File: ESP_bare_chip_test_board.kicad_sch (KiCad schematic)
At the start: 0 parts

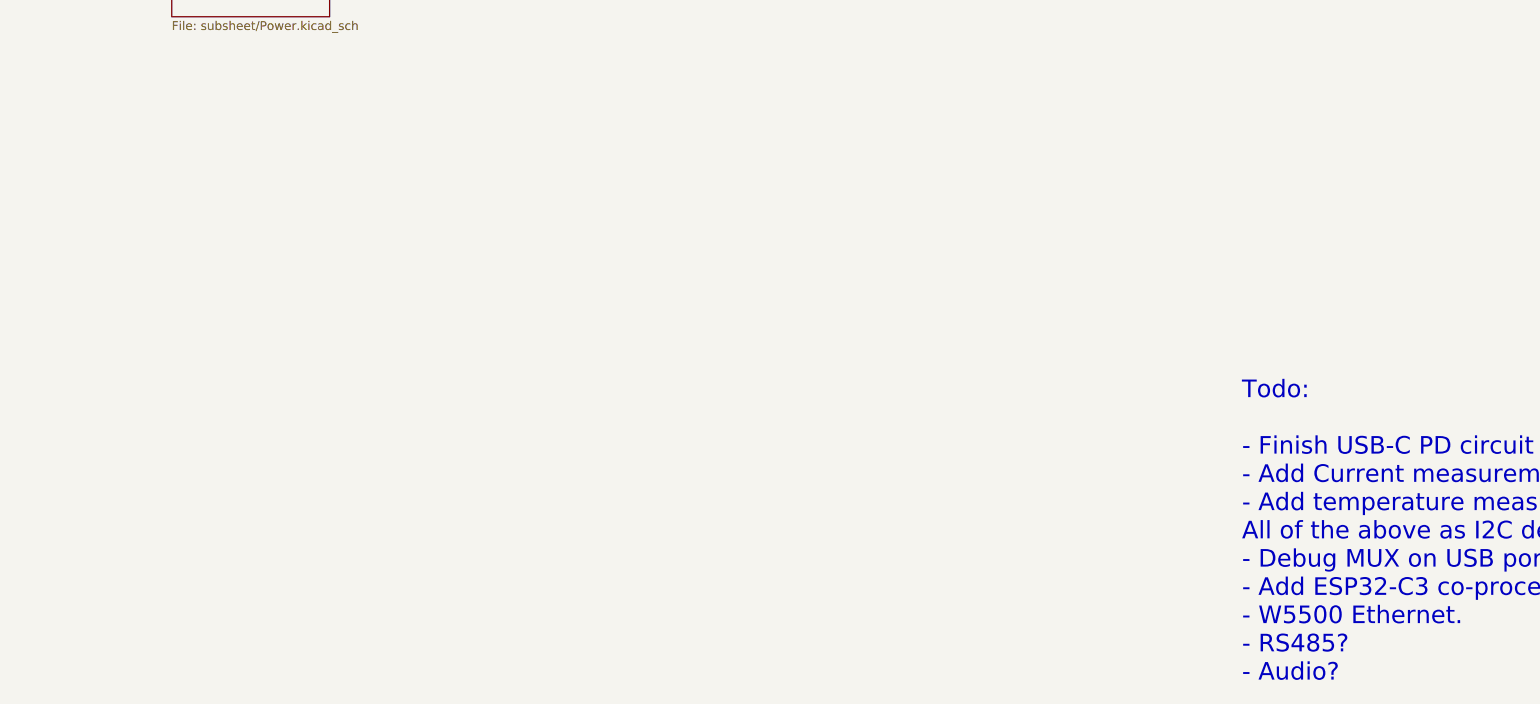
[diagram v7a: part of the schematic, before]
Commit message: Replace buck-regulator with buck-boost regulator
Replaced the buck-regulator with a buck-boost regulator. The primary
purpose is because the buck-regulator could fail when a higher-voltage
output was conected. The buck-regulators internal switches and design
should be much less vulnerable for this.

A second benefit of the buck-boost regulator is thata 5V input can now
still be used, as it accounts for the voltage-drop from the
bridge-rectifier diodes.
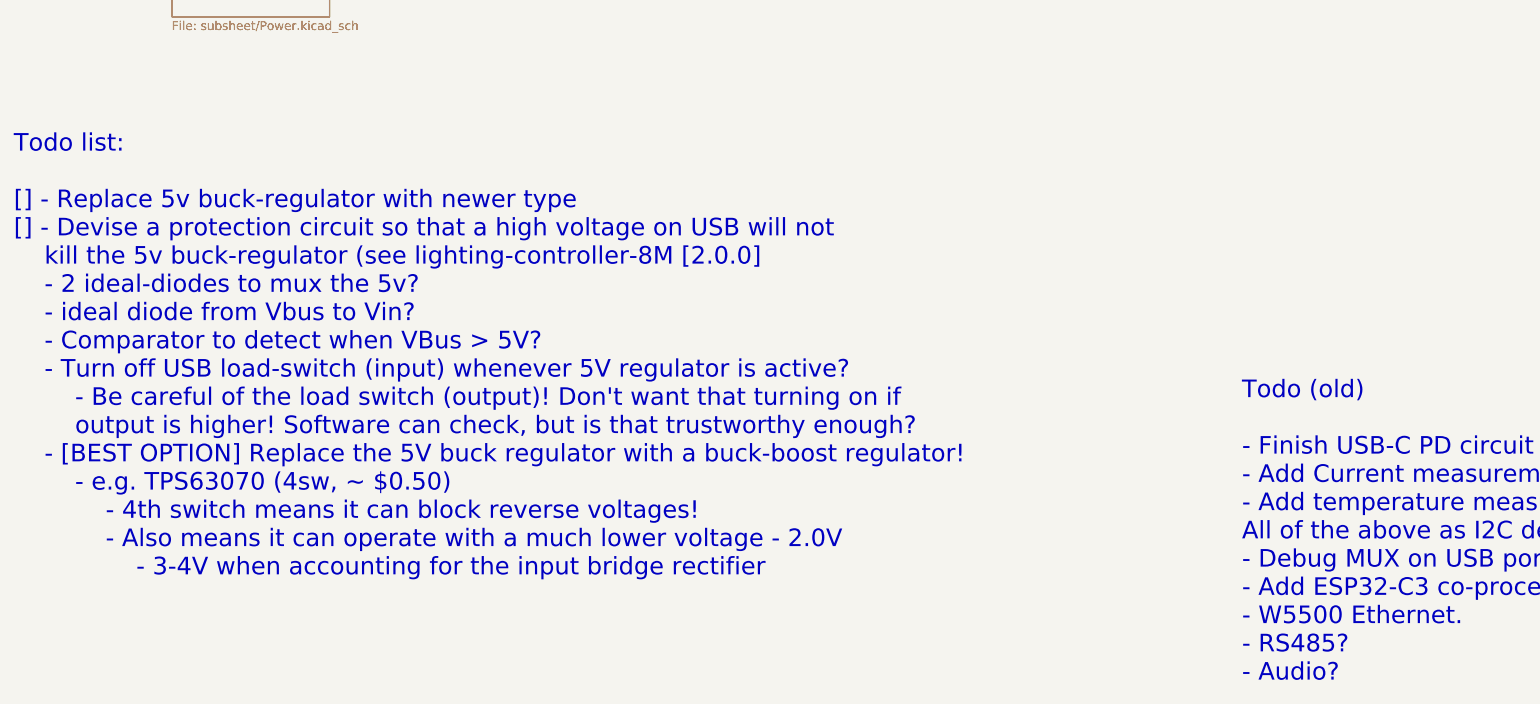
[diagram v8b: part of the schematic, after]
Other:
- note added: "Todo (old) - Finish USB-C PD circuit - Add Current measurement IC - Add temperature measurment IC All of the above as I2C devices :) - Debug MUX on USB port? - Add ESP32-C3 co-processor? - W5500 Ethernet. - RS485? - Audio?"
- note added: "Todo list: [] - Replace 5v buck-regulator with newer type [] - Devise a protection circuit so that a high voltage on USB will not kill the 5v buck-regulator (see lighting-controller-8M [2.0.0] - 2 ideal-diodes to mux the 5v? - ideal diode from Vbus to Vin? - Comparator to detect when VBus > 5V? - Turn off USB load-switch (input) whenever 5V regulator is active? - Be careful of the load switch (ou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"
- note removed: "Todo: - Finish USB-C PD circuit - Add Current measurement IC - Add temperature measurment IC All of the above as I2C devices :) - Debug MUX on USB port? - Add ESP32-C3 co-processor? - W5500 Ethernet. - RS485? - Audio?"
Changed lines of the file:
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@@
 		)
 	)
-	(text "Todo:\n\n- Finish USB-C PD circuit\n- Add Current measurement IC\n- Add temperature measurment IC\nAll of the above as I2C devices :)\n- Debug MUX on USB port?\n- Add ESP32-C3 co-processor?\n- W5500 Ethernet.\n- RS485?\n- Audio?"
+	(text "Todo (old)\n\n- Finish USB-C PD circuit\n- Add Current measurement IC\n- Add temperature measurment IC\nAll of the above as I2C devices :)\n- Debug MUX on USB port?\n- Add ESP32-C3 co-processor?\n- W5500 Ethernet.\n- RS485?\n- Audio?"
 		(exclude_from_sim no)
 		(at 175.26 279.4 0)
@@
 			)
 			(justify left bottom)
+		)
+	)
+	(text "Todo list:\n\n[] - Replace 5v buck-regulator with newer type\n[] - Devise a protection circuit so that a high voltage on USB will not\n	kill the 5v buck-regulator (see lighting-controller-8M [2.0.0]\n	- 2 ideal-diodes to mux the 5v?\n	- ideal diode from Vbus to Vin?\n	- Comparator to detect when VBus > 5V?\n	- Turn off USB load-switch (input) whenever 5V regulator is active?\n		- Be careful of the load switch (output)! Don't want that turning on if\n		output is higher! Software can check, but is that trustworthy enough?\n	- [BEST OPTION] Replace the 5V buck regulator with a buck-boost regulator!\n		- e.g. TPS63070 (4sw, ~ $0.50)\n			- 4th switch means it can block reverse voltages!\n			- Also means it can operate with a much lower voltage - 2.0V\n				- 3-4V when accounting for the input bridge rectifier"
+		(exclude_from_sim no)
+		(at -2.54 264.16 0)
+		(effects
+			(font
+				(size 2.54 2.54)
+			)
+			(justify left bottom)
